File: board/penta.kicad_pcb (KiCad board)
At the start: 4 copper layers, 37.4 x 37.4 mm, 144 parts, among them J1 USB_C_Receptacle_PowerOnly_6P, Q1 SK335N, U1 XIAO-RP2040-SMD

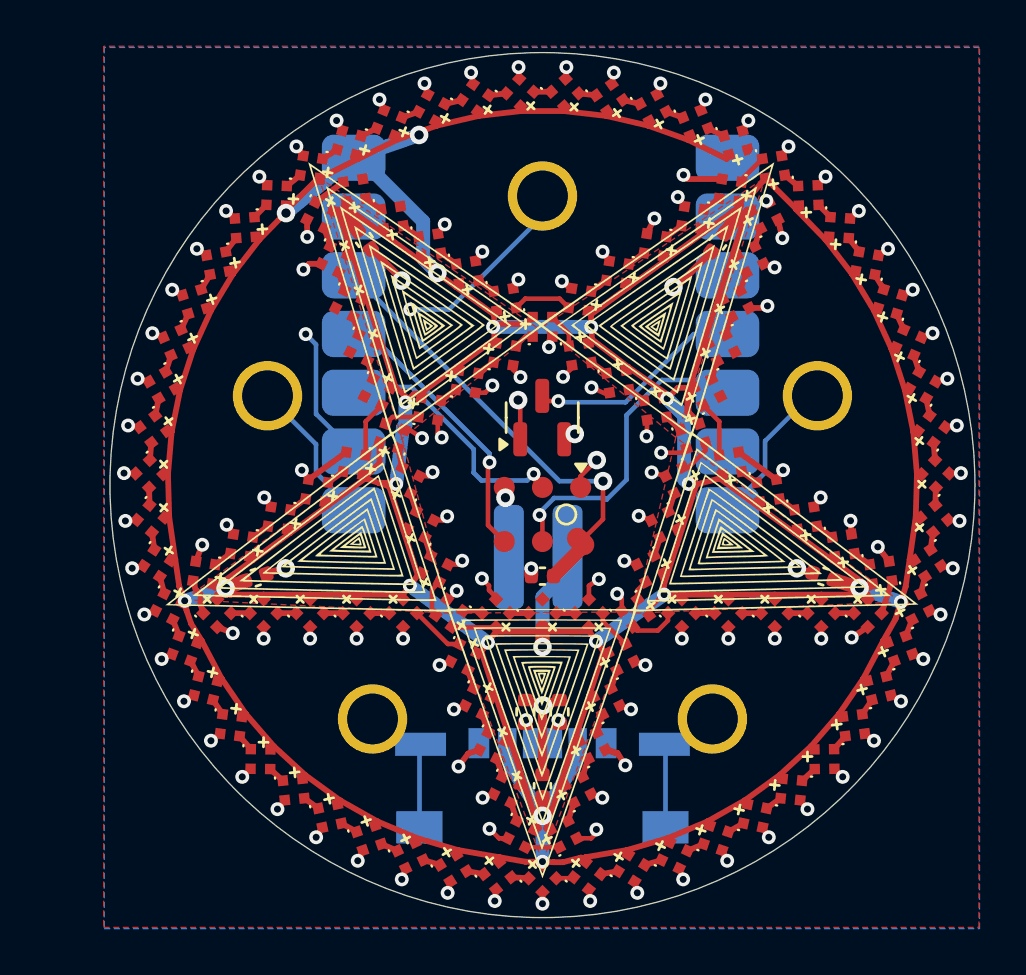
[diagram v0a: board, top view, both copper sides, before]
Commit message: ok. support all 5 touch pins because we can
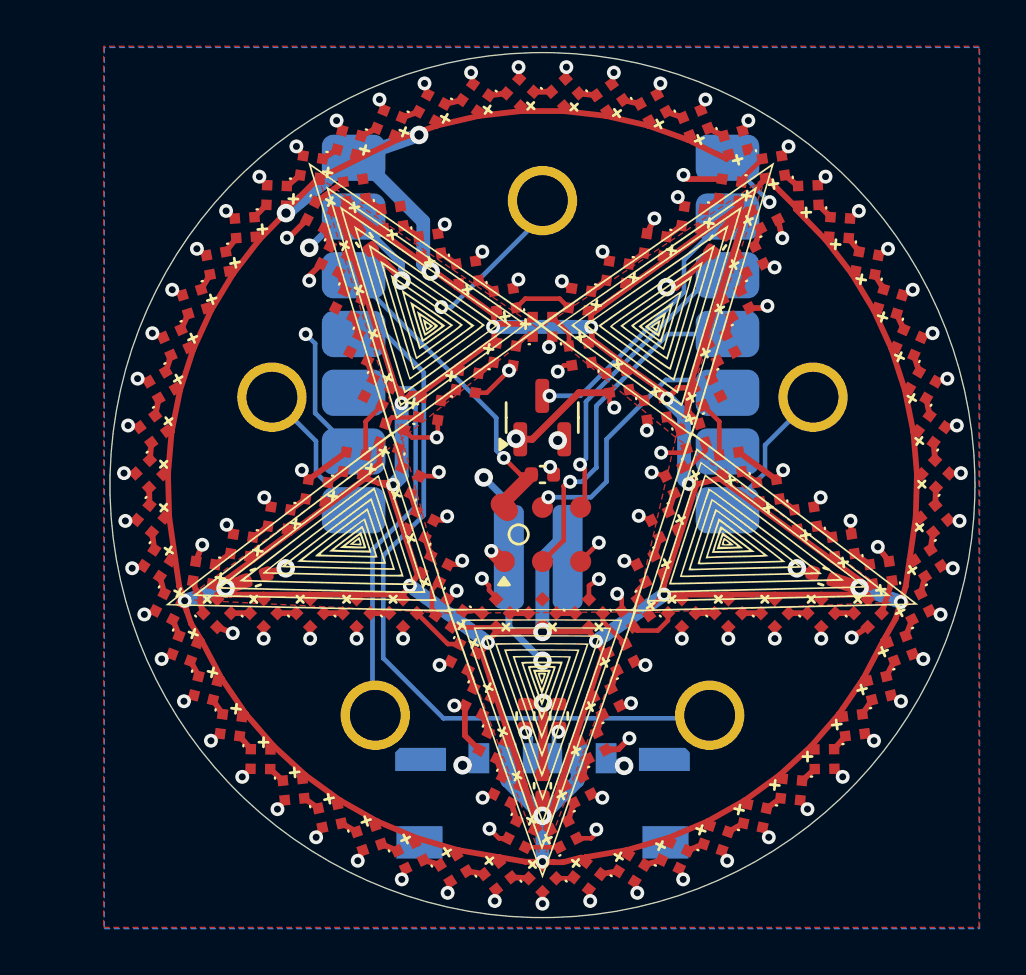
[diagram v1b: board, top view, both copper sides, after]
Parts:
- C20, C21, C22, C23, C24: value 10u -> 10uF
- moved C1 4.39 mm to (100.0, 99.5), turned to 0 degrees
- moved MIC1 0.86 mm to (100.0, 102.1), turned to 0 degrees
- moved J1 0.65 mm to (100.0, 113.6)
- moved TP2 0.20 mm to (100.0, 87.7)
- moved TP3 0.20 mm to (107.2, 110.0)
- moved TP4 0.20 mm to (92.8, 110.0)
- moved TP0 0.20 mm to (111.7, 96.2)
- moved TP1 0.20 mm to (88.3, 96.2)
- moved R1 0.18 mm to (100.7, 110.0)
- moved R2 0.18 mm to (99.3, 110.0)
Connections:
- J1 pad S1: Net-(J1-SHIELD) -> unconnected-(J1-SHIELD-PadS1)_1
- TP3 pad 1: Net-(J1-SHIELD) -> /TOUCH3
- TP4 pad 1: Net-(J1-SHIELD) -> /TOUCH4
- U1 pad 1: unconnected-(U1-GPIO26_A0_D0-Pad1) -> /LED_DATA
- U1 pad 10: /LRCLK -> /TOUCH4
- U1 pad 11: /BCLK -> /TOUCH3
- U1 pad 2: /LED_DATA -> /EN_PIXELS
- U1 pad 3: unconnected-(U1-GPIO28_A2_D2-Pad3) -> /BCLK
- U1 pad 4: /EN_PIXELS -> /LRCLK
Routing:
- net /TOUCH3: track 0.00 -> 32.0 mm
- net /TOUCH4: track 0.00 -> 17.6 mm
- net GND: track 13.0 -> 29.8 mm, vias 9 -> 14
- net Net-(J1-SHIELD): track 7.22 -> 0.00 mm
- net +3V3: track 19.5 -> 14.1 mm
- net /PXL_GND: track 75.2 -> 80.5 mm, vias 116 -> 113
- net /LRCLK: track 11.0 -> 15.0 mm
- net /EN_PIXELS: track 9.35 -> 12.0 mm
- net +5V: track 307.1 -> 304.7 mm
- net /I2S DATA: track 13.7 -> 11.7 mm
- net /BCLK: track 12.1 -> 13.2 mm
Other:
- board text added: "EN"
- board text added: "T3"
- board text added: "T4"
- board text removed: "EN_LED"

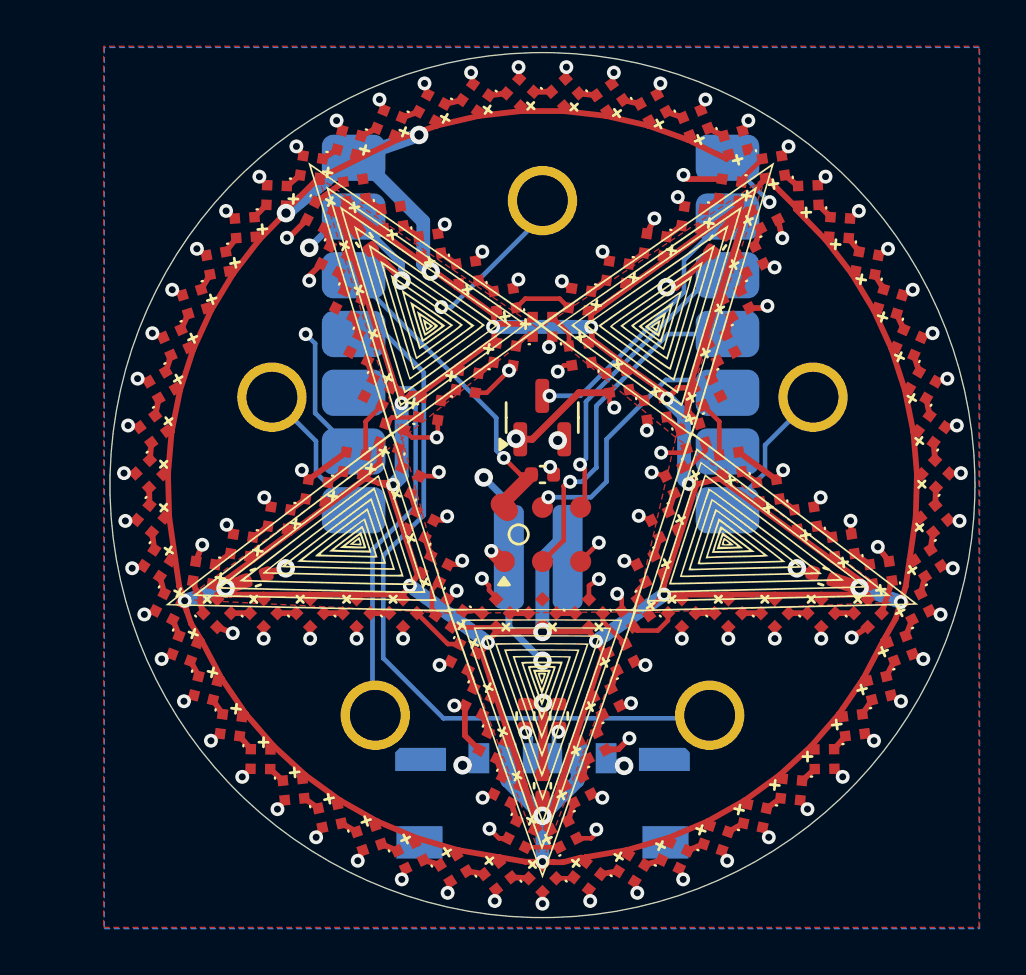
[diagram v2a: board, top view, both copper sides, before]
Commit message: drop in an rp2040 and associated circuitry; proper usb port (two of them); bottom-facing mic; do a first pass on layout
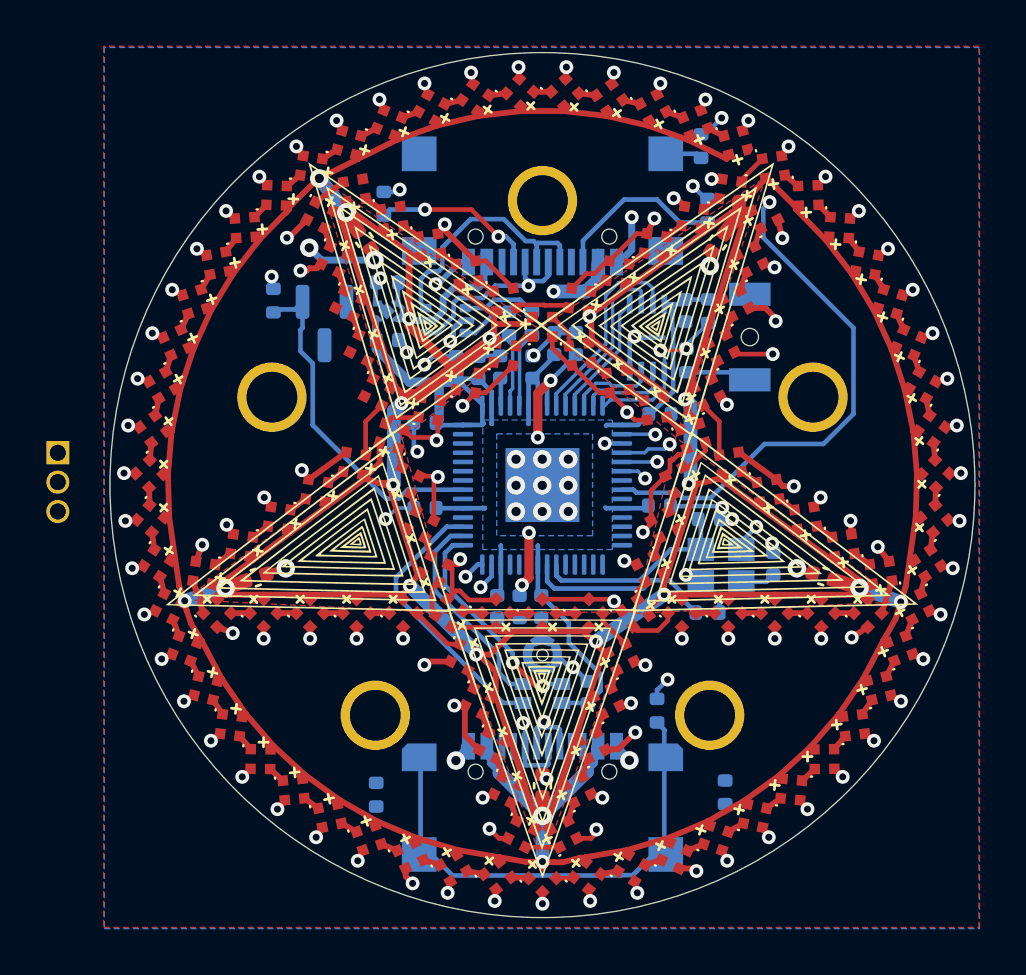
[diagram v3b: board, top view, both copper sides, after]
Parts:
- removed MIC1: LMD4737T263-OY1, penta:LGA-6_L4.7-W3.8-P1.65_LMD4737T
- added C10: 100nF, Capacitor_SMD:C_0402_1005Metric, B.Cu at (96.3, 94.9)
- added C11: 100nF, Capacitor_SMD:C_0402_1005Metric, B.Cu at (99.6, 94.9)
- added C12: 1uF, Capacitor_SMD:C_0402_1005Metric, B.Cu at (98.2, 94.9)
- added C13: 1uF, Capacitor_SMD:C_0402_1005Metric, B.Cu at (97.2, 94.9)
- added C14: 12pF, Capacitor_SMD:C_0402_1005Metric, B.Cu at (107.2, 101.5)
- added C15: 12pF, Capacitor_SMD:C_0402_1005Metric, B.Cu at (110.0, 103.4)
- added C16: 1uF, Capacitor_SMD:C_0402_1005Metric, B.Cu at (93.3, 91.2)
- added C17: 100nF, Capacitor_SMD:C_0402_1005Metric, B.Cu at (106.2, 92.5)
- added C18: 1uF, Capacitor_SMD:C_0402_1005Metric, B.Cu at (93.3, 93.7)
- added C19: 100nF, Capacitor_SMD:C_0402_1005Metric, B.Cu at (105.1, 96.9)
- added C2: 100nF, Capacitor_SMD:C_0402_1005Metric, B.Cu at (99.0, 105.3)
- added C3: 100nF, Capacitor_SMD:C_0402_1005Metric, B.Cu at (101.4, 93.9)
- added C4: 100nF, Capacitor_SMD:C_0402_1005Metric, B.Cu at (94.9, 97.3)
- added C5: 100nF, Capacitor_SMD:C_0402_1005Metric, B.Cu at (105.1, 100.9)
- added C6: 100nF, Capacitor_SMD:C_0402_1005Metric, B.Cu at (98.0, 105.3)
- added C7: 100nF, Capacitor_SMD:C_0402_1005Metric, B.Cu at (100.5, 93.9)
- added C8: 100nF, Capacitor_SMD:C_0402_1005Metric, B.Cu at (99.9, 105.3)
- added C9: 100nF, Capacitor_SMD:C_0402_1005Metric, B.Cu at (94.9, 101.0)
- added J2: USB_C_Receptacle, penta:USB-SMD_USB-TYPE-C-020, B.Cu at (100.0, 88.0)
- added J3: Conn_01x03_Pin, Connector_PinSocket_1.27mm:PinSocket_1x03_P1.27mm_Vertical, B.Cu at (79.0, 98.6)
- added MIC2: T3902, penta:MIC-SMD_5P-L3.5-W2.7-TL_MMICT390200012, B.Cu at (100.0, 108.1)
- added R10: 1k, Resistor_SMD:R_0402_1005Metric, B.Cu at (107.1, 105.5)
- added R11: 1M, Resistor_SMD:R_0402_1005Metric, B.Cu at (105.0, 109.8)
- added R12: 10k, Resistor_SMD:R_0402_1005Metric, B.Cu at (88.4, 92.0)
- added R14: 10k DNF, Resistor_SMD:R_0402_1005Metric, B.Cu at (107.2, 92.5)
- added R3: 27, Resistor_SMD:R_0402_1005Metric, B.Cu at (99.5, 93.0)
- added R5: 5.11K, Resistor_SMD:R_0402_1005Metric, B.Cu at (93.1, 87.8)
- added R6: 27, Resistor_SMD:R_0402_1005Metric, B.Cu at (98.6, 93.0)
- added R7: 5.11K, Resistor_SMD:R_0402_1005Metric, B.Cu at (107.1, 88.1)
- added R8: 1M, Resistor_SMD:R_0402_1005Metric, B.Cu at (106.9, 85.3)
- added R9: 1k, Resistor_SMD:R_0402_1005Metric, B.Cu at (106.2, 94.6)
- added SW1: SW_Push, penta:KEY-SMD_L3.0-W2.5-LS4.0, B.Cu at (109.0, 93.6)
- added U2: RP2040, Package_DFN_QFN:QFN-56-1EP_7x7mm_P0.4mm_EP3.2x3.2mm, B.Cu at (100.0, 100.0)
- added U3: QSPI Flash, penta:USON_3X2_WIN, B.Cu at (104.5, 93.6)
- added U5: USBLC6-2P6, Package_TO_SOT_SMD:SOT-666, B.Cu at (95.8, 92.9)
- added Y1: 12MHz, Crystal:Crystal_SMD_2520-4Pin_2.5x2.0mm, B.Cu at (107.7, 103.5)
- C1, R1, R2: moved to B.Cu
- J1: value USB_C_Receptacle_PowerOnly_6P -> USB_C_Receptacle; footprint penta:USB-C-SMD_TYPE-C-6P-QT073 -> penta:USB-SMD_USB-TYPE-C-020
- Q1: value SK335N -> Q_NMOS_GSD; moved to B.Cu
- U1: value XIAO-RP2040-SMD -> 3.3V LDO; footprint penta:XIAO-RP2040-SMD -> Package_DFN_QFN:OnSemi_XDFN4-1EP_1.0x1.0mm_EP0.52x0.52mm
- moved Q1 10.3 mm to (90.6, 93.0), turned to -90 degrees
- moved G*** 9.75 mm to (91.6, 102.7)
- moved C1 9.62 mm to (102.0, 109.0), turned to 90 degrees
- moved R2 9.25 mm to (107.9, 113.3)
- moved R1 8.60 mm to (92.8, 113.4)
- moved U1 6.81 mm to (93.3, 92.5), turned to 0 degrees
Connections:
- J1 pad S1: unconnected-(J1-SHIELD-PadS1)_1 -> Net-(J1-SHIELD)
- Q1 pad 1: /PXL_GND -> /EN_PIXELS
- Q1 pad 3: /EN_PIXELS -> /PXL_GND
- TP0 pad 1: /TOUCH0 -> Net-(U2-GPIO0)
- TP1 pad 1: /TOUCH1 -> Net-(U2-GPIO2)
- TP2 pad 1: /TOUCH2 -> Net-(U2-GPIO1)
- TP3 pad 1: /TOUCH3 -> Net-(U2-GPIO4)
- TP4 pad 1: /TOUCH4 -> Net-(U2-GPIO3)
- U1 pad 1: /LED_DATA -> +3V3
- U1 pad 2: /EN_PIXELS -> GND
- U1 pad 3: /BCLK -> +5V
- U1 pad 4: /LRCLK -> +5V
- U1 pad 5: /I2S DATA -> GND
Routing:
- net Net-(U2-GPIO2): track 0.00 -> 73.2 mm, vias 0 -> 1
- net Net-(U2-GPIO3): track 0.00 -> 51.4 mm, vias 0 -> 1
- net /TOUCH3: track 32.0 -> 0.00 mm
- net +3V3: track 14.1 -> 45.6 mm, vias 1 -> 0
- net Net-(U2-GPIO1): track 0.00 -> 31.0 mm, vias 0 -> 1
- net Net-(U2-GPIO4): track 0.00 -> 28.6 mm, vias 0 -> 1
- net Net-(J1-SHIELD): track 0.00 -> 20.8 mm
- net /LED_DATA: track 2.67 -> 22.6 mm
- net /TOUCH2: track 19.0 -> 0.00 mm, vias 2 -> 0
- net /PXL_GND: track 80.5 -> 98.2 mm, vias 113 -> 101
- net /TOUCH4: track 17.6 -> 0.00 mm
- net /LRCLK: track 15.0 -> 0.00 mm, vias 1 -> 0
- net /BCLK: track 13.2 -> 0.00 mm, vias 1 -> 0
- net /USB2_D+: track 0.00 -> 12.2 mm, vias 0 -> 2
- net /PDM_DATA: track 0.00 -> 12.0 mm
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- added copper zone on B.Cu, net +1V1
- added copper zone on B.Cu, net +3V3
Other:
- board text removed: "+5V"
- board text removed: "3.3V"
- board text removed: "BCLK"
- board text removed: "EN"
- board text removed: "GND"
- board text removed: "I2SD"
- board text removed: "LED"
- board text removed: "LRCLK"
- board text removed: "T0"
- board text removed: "T1"
- board text removed: "T2"
- board text removed: "T3"
- board text removed: "T4"
- board text removed: "seeed xiao rp2040"

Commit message: add a usb mux for communicating between pentas and make a draft layout
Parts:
- added C25: 100nF, Capacitor_SMD:C_0402_1005Metric, B.Cu at (92.2, 94.0)
- added R13: 27, Resistor_SMD:R_0402_1005Metric, B.Cu at (95.1, 109.0)
- added R15: 10k, Resistor_SMD:R_0402_1005Metric, B.Cu at (85.6, 93.2)
- added R16: 27, Resistor_SMD:R_0402_1005Metric, B.Cu at (90.3, 94.0)
- added R4: 27, Resistor_SMD:R_0402_1005Metric, B.Cu at (96.2, 109.0)
- added U4: MSUSB30, Package_SO:MSOP-10_3x3mm_P0.5mm, B.Cu at (89.4, 91.8)
- J3: footprint Connector_PinSocket_1.27mm:PinSocket_1x03_P1.27mm_Vertical -> penta:SMD_Pad_01x03_1.27mm
- moved G*** 23.6 mm to (115.1, 100.1), turned to -30 degrees
- moved J3 23.2 mm to (100.0, 108.7)
- moved R2 14.8 mm to (94.2, 107.7)
- moved R1 14.4 mm to (106.0, 107.5), turned to 180 degrees
- moved C1 12.2 mm to (90.8, 104.0), turned to 180 degrees
- moved R12 10.2 mm to (92.9, 101.1), turned to -90 degrees
- moved MIC2 8.33 mm to (91.8, 106.3), turned to 180 degrees
- moved Q1 8.15 mm to (90.4, 101.2), turned to 180 degrees
- moved C18 4.18 mm to (91.8, 97.6), turned to 180 degrees
- moved C16 4.13 mm to (91.9, 95.1)
- moved U1 4.08 mm to (92.0, 96.4)
- moved R8 1.91 mm to (106.8, 87.2), turned to 90 degrees
- moved U5 1.22 mm to (94.6, 92.8), turned to 90 degrees
- moved R7 1.09 mm to (106.8, 89.2)
- moved C8 0.92 mm to (100.4, 106.1)
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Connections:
- R7 pad 1: Net-(J2-CC2) -> GND
- R7 pad 2: GND -> Net-(J2-CC2)
- U2 pad 27: /USB2_D- -> /UART0_TX
- U2 pad 28: /USB2_D+ -> /UART0_RX
- U2 pad 34: unconnected-(U2-GPIO22-Pad34) -> /EN_PIXELS
- U2 pad 35: /EN_PIXELS -> /USBMUX_SELECT
- U2 pad 36: unconnected-(U2-GPIO24-Pad36) -> /UART1_TX
- U2 pad 37: unconnected-(U2-GPIO25-Pad37) -> /UART1_RX
- U5 pad 1: /USB_D+ -> /USB_D+_PORT
- U5 pad 3: /USB_D- -> /USB_D-_PORT
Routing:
- net Net-(U2-GPIO0): track 8.94 -> 40.1 mm
- net /UART1_RX: track 0.00 -> 19.7 mm
- net /PXL_GND: track 98.2 -> 116.7 mm
- net /USBMUX_SELECT: track 0.00 -> 18.2 mm, vias 0 -> 2
- net /UART1_TX: track 0.00 -> 17.7 mm
- net GND: track 40.9 -> 54.5 mm, vias 38 -> 51
- net +3V3: track 45.6 -> 58.0 mm
- net /USB_D+_PORT: track 0.00 -> 10.7 mm
- net /USB_D+: track 3.25 -> 13.7 mm, vias 0 -> 2
- net Net-(U2-GPIO4): track 28.6 -> 38.6 mm
- net /USB_D-: track 2.27 -> 12.2 mm, vias 0 -> 2
- net /EN_PIXELS: track 15.0 -> 5.42 mm
- net /SWCLK: track 0.00 -> 7.04 mm
- net Net-(J1-CC1): track 0.00 -> 6.88 mm
- net Net-(J1-CC2): track 0.00 -> 6.54 mm
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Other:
- board text added: "CLK"
- board text added: "G"
- board text added: "SWD"

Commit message: polish & readiness
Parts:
- added TP5: TestPoint, TestPoint:TestPoint_Pad_D1.0mm, B.Cu at (86.3, 99.4)
- MIC2: footprint penta:MIC-SMD_5P-L3.5-W2.7-TL_MMICT390200012 -> penta:MIC_T3902
- moved SW1 1.47 mm to (110.3, 93.0), turned to 0 degrees
- moved R13 0.18 mm to (95.1, 108.8)
- moved R4 0.18 mm to (96.2, 108.8)
- moved C1 0.16 mm to (90.9, 103.9)
- moved J1 0.12 mm to (100.0, 113.5)
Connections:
- U2 pad 38: unconnected-(U2-GPIO26_ADC0-Pad38) -> Net-(U2-GPIO26_ADC0)
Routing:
- net Net-(U2-GPIO1): track 31.6 -> 45.6 mm
- net Net-(U2-GPIO26_ADC0): track 0.00 -> 11.4 mm, vias 0 -> 2
- net +3V3: track 58.0 -> 52.8 mm
- net /LED_DATA: track 22.6 -> 17.4 mm
- net Net-(U2-GPIO4): track 38.6 -> 42.5 mm
- net GND: track 54.5 -> 52.6 mm
- net (no net): track 0.00 -> 1.74 mm, vias 0 -> 1
- net /PXL_GND: track 116.7 -> 115.2 mm, vias 101 -> 100
- net Net-(U2-XOUT): track 9.61 -> 8.30 mm
- net Net-(U2-XIN): track 10.1 -> 9.41 mm
- net +5V: track 307.7 -> 308.3 mm
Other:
- board text added: "26"
- board text added: "USB"
